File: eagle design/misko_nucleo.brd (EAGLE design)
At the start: 70 x 82.5 mm, 44 parts, among them IC1101 47309-2651, IC1201 FM25W256, IC1301 ADXL345, IC1302 74HCT1G32GW, IC401 TCAN334, J1 CAN, Q1701 SQ2310ES-T1_BE3, Q1702 SQ2310ES-T1_BE3, Q1703 SQ2310ES-T1_BE3

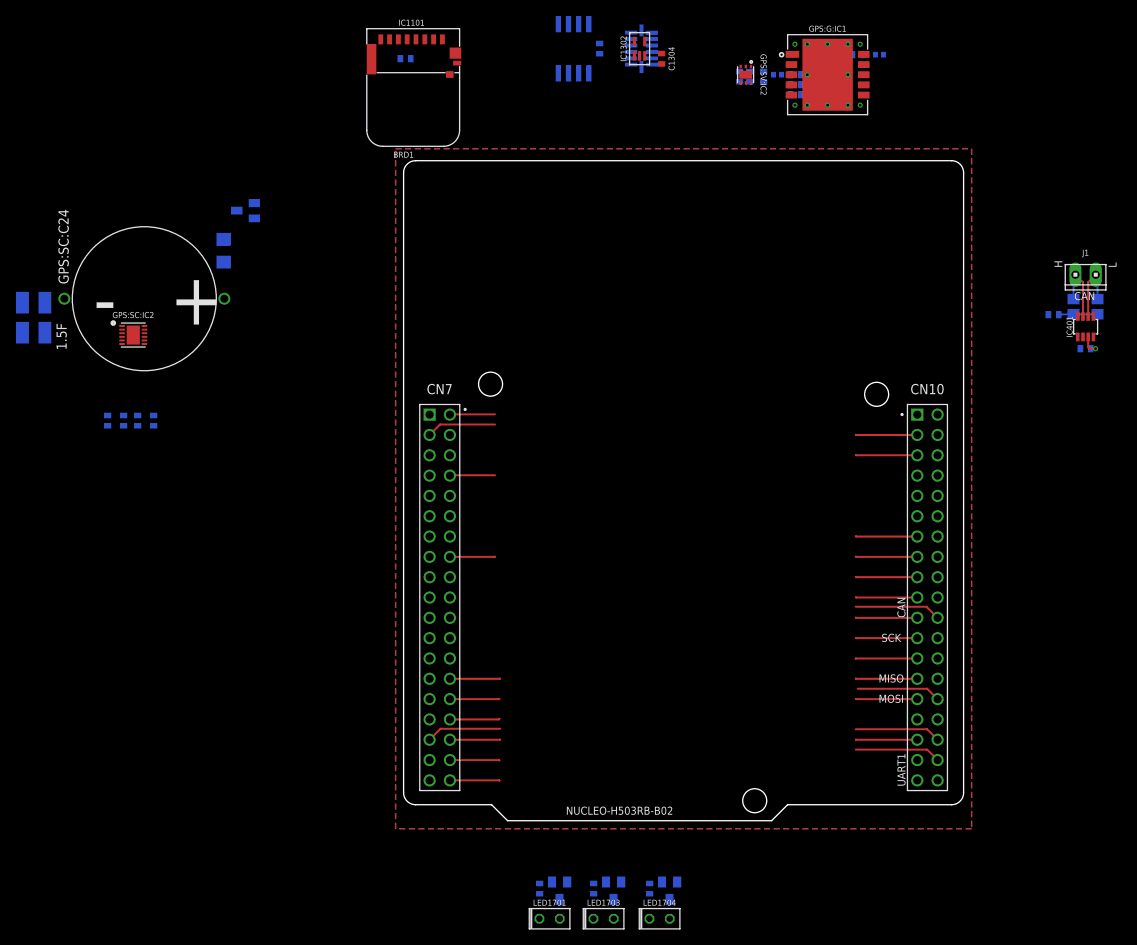
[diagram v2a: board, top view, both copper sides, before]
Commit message: board rev.3 on nucleo - connected & routed a nucleo H503RB-B02 compatible sch & brd - moved GPIOs to better suited physical locations - added yellow LED - sent board to the fab
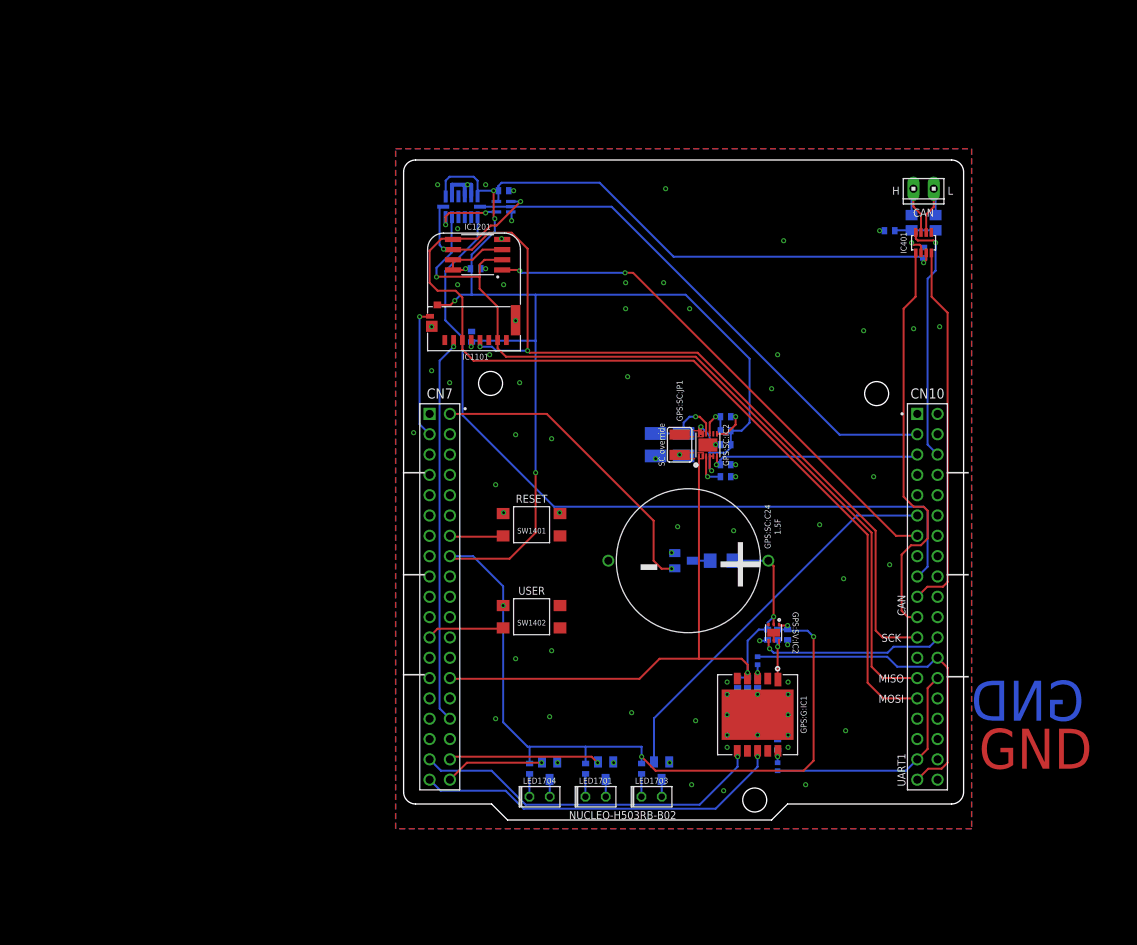
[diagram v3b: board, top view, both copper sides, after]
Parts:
- added GPS:SC:JP1: SC override, jumper:SJW
- added GPS:SC:R2: 10k, resistor:R0402
- added SW1401, SW1402: TL3305CF160QG, TL3305-844809 SPST-NO Tact Switch:SMD
- moved GPS:G:R2 89.9 mm to (46.8, 6.75), turned to 90 degrees
- moved GPS:G:C31 86.8 mm to (46.8, 9.50), turned to 90 degrees
- moved GPS:SC:C34 83.2 mm to (35.0, 47.0), turned to 90 degrees
- moved GPS:G:IC1 80.5 mm to (44.2, 13.2), turned to 270 degrees
- moved GPS:SC:C1 79.0 mm to (31.5, 47.0), turned to 270 degrees
- moved GPS:SC:R14 77.6 mm to (40.2, 43.0), turned to 0 degrees
- moved GPS:G:C22 76.1 mm to (44.2, 17.2), turned to 270 degrees
- moved GPS:SC:C24 75.5 mm to (35.8, 32.5)
- moved GPS:SC:C38 75.3 mm to (40.2, 47.0), turned to 0 degrees
- moved GPS:G:C2 75.0 mm to (43.0, 17.2), turned to 270 degrees
- moved GPS:G:C1 73.9 mm to (41.8, 17.2), turned to 270 degrees
- moved GPS:SC:R41 73.5 mm to (40.2, 50.5), turned to 0 degrees
- moved GPS:SC:R1 73.3 mm to (39.8, 32.5), turned to 180 degrees
- moved GPS:G:R1 73.3 mm to (44.2, 20.0), turned to 270 degrees
- moved GPS:SC:IC2 73.1 mm to (38.0, 47.0), turned to 90 degrees
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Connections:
- net GPS:SC:N$1 renamed GPS:SC:SC_DIS_DRAIN
- removed net GPS:SV:CT: GPS:SV:IC2.CT
- removed net GPS:VGPS: GPS:G:C1.1, GPS:G:C2.1, GPS:G:IC1.4_VCC, GPS:SC:C24.+, GPS:SC:C34.1, GPS:SC:IC2.VOUT1, GPS:SC:IC2.VOUT2, GPS:SC:R1.2, GPS:SV:C1.1, GPS:SV:IC2.SENSE
- removed net GPS_YELLOW_LED: BRD1.CN7_23
- removed net PA5: BRD1.CN10_11
- removed net PB1: BRD1.CN10_24
- removed net PC2: BRD1.CN7_35
- removed net PC3: BRD1.CN7_37
- removed net PC5: BRD1.CN10_6
- new net PA10: BRD1.CN10_33
- new net PA7: BRD1.CN10_15
- new net PB0: BRD1.CN7_34
- new net PB12: BRD1.CN10_16
- new net PC4: BRD1.CN10_34
- new net USER_BUTTON: BRD1.CN7_23, SW1402.1, SW1402.2
- net 3V3: now also GPS:SC:JP1.2, SW1402.3, SW1402.4
- net ADC_VGPS: now also GPS:G:C1.1, GPS:G:C2.1, GPS:G:IC1.4_VCC, GPS:SC:C24.+, GPS:SC:C34.1, GPS:SC:IC2.VOUT1, GPS:SC:IC2.VOUT2, GPS:SC:JP1.1, GPS:SC:R1.2, GPS:SV:C1.1, GPS:SV:IC2.SENSE
- net ADXL345_CS: now also BRD1.CN10_3; no longer BRD1.CN10_15
- net CAN_!STBY!: now also BRD1.CN10_6; no longer BRD1.CN10_16
- net GND: now also GPS:SC:R2.1, SW1401.3, SW1401.4
- net GPS_!RESET!: now also BRD1.CN7_37; no longer BRD1.CN10_3
- net GPS_PWR_CTRL: now also BRD1.CN10_24; no longer BRD1.CN10_34
- net GPS_WKUP: now also BRD1.CN7_35; no longer BRD1.CN10_33
- net LED_GREEN: now also BRD1.CN10_11; no longer BRD1.CN7_2
- net LED_RED: now also BRD1.CN7_38; no longer BRD1.CN7_3
- net LED_YELLOW: now also BRD1.CN7_36; no longer BRD1.CN7_38
- net NRST: now also SW1401.1, SW1401.2
- net SD_CD: now also BRD1.CN7_3; no longer BRD1.CN7_34
- net SPI1_MISO: no longer IC1101.CMD
- net SPI1_MOSI: now also IC1101.CMD
- net SUPERCAP_!EN!: now also GPS:SC:R2.2
- net SUPERCAP_DISCHARGE: now also BRD1.CN7_2; no longer BRD1.CN7_36
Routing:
- net 3V3: track 8.55 -> 313.4 mm, vias 1 -> 13
- net SPI1_MOSI: track 7.71 -> 116.4 mm, vias 0 -> 1
- net SPI1_SCK: track 7.71 -> 108.8 mm, vias 0 -> 3
- net SPI1_MISO: track 7.71 -> 107.5 mm, vias 0 -> 1
- net ADXL345_INT1: track 7.71 -> 99.2 mm
- net ADC_VGPS: track 6.29 -> 89.8 mm, vias 0 -> 3
- net ADXL345_CS: track 7.71 -> 66.5 mm
- net SPI1_FRAM_CS: track 7.71 -> 65.7 mm, vias 0 -> 2
- net CAN_TX: track 7.71 -> 51.7 mm
- net LED_GREEN: track 5.66 -> 48.9 mm
- net SPI1_SD_CS: track 6.25 -> 48.6 mm, vias 0 -> 1
- net GPS_MCU_TX: track 0.00 -> 41.8 mm
- net GPS_!RESET!: track 7.71 -> 46.7 mm, vias 0 -> 1
- net CAN_RX: track 7.71 -> 46.5 mm
- net GPS_WKUP: track 7.71 -> 44.8 mm, vias 0 -> 1
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- added copper zone on layer 1, net 3V3
- added copper zone on layer 1, net ADC_VGPS
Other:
- board text added: "GND"
- board text added: "RESET"
- board text added: "SC override"
- board text added: "USER"
- board text added: "docu"
- board text added: "|"
- board text removed: "info"

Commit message: - added BOM to rev3 board
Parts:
- C405: value 0.1uF / 10V -> 0.1u / 16V
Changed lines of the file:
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@@
 <attribute name="VALUE" x="67" y="72.25" size="0.5" layer="27" font="vector" rot="R90" align="center"/>
 </element>
-<element name="C405" library="rcl" library_urn="urn:adsk.eagle:library:334" package="C0402" package3d_urn="urn:adsk.eagle:package:23626/2" value="0.1uF / 10V" x="65" y="71" smashed="yes" rot="MR90">
+<element name="C405" library="rcl" library_urn="urn:adsk.eagle:library:334" package="C0402" package3d_urn="urn:adsk.eagle:package:23626/2" value="0.1u / 16V" x="65" y="71" smashed="yes" rot="MR90">
 <attribute name="NAME" x="63.75" y="71" size="0.75" layer="26" font="vector" rot="MR90" align="center"/>
 <attribute name="POPULARITY" value="18" x="65" y="71" size="0.75" layer="28" font="vector" rot="MR90" display="off"/>

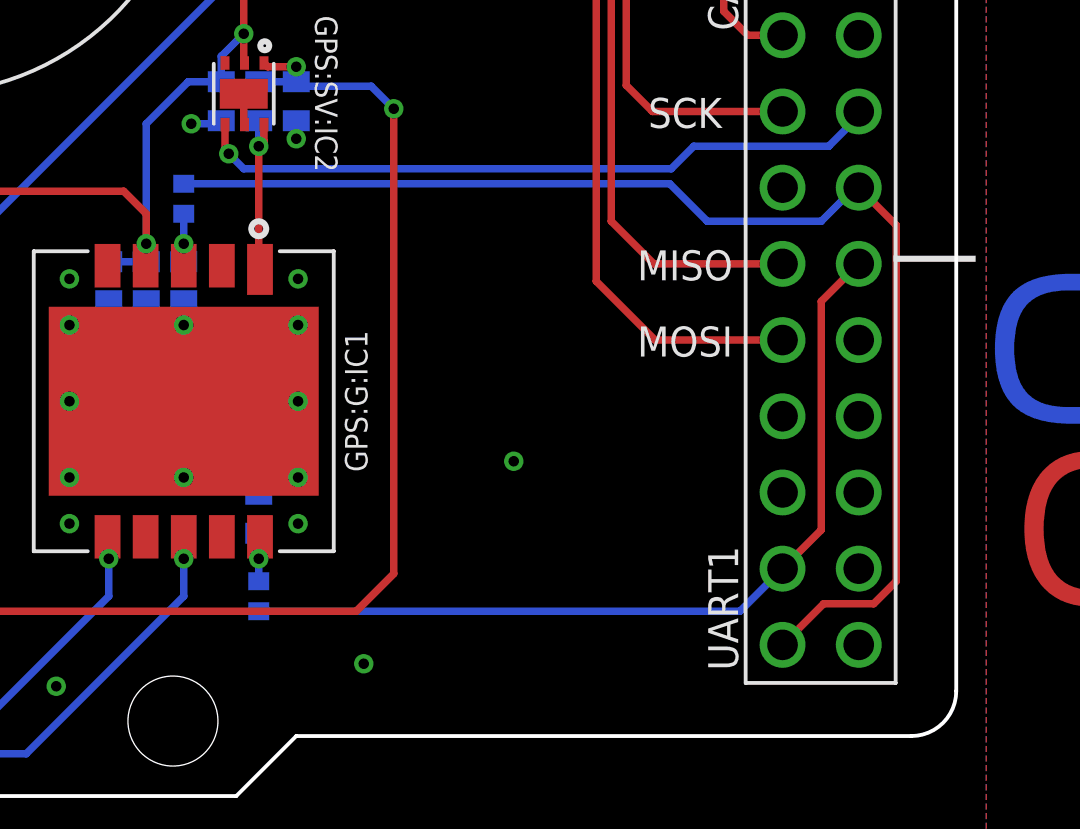
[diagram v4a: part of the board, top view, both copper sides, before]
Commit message: minor corrections for rev.3 board: - corrected UART1 lines towards board - added debug and attach launch configs - adapted code to match rev.3 board
- corrected BOM items
- renamed BOM
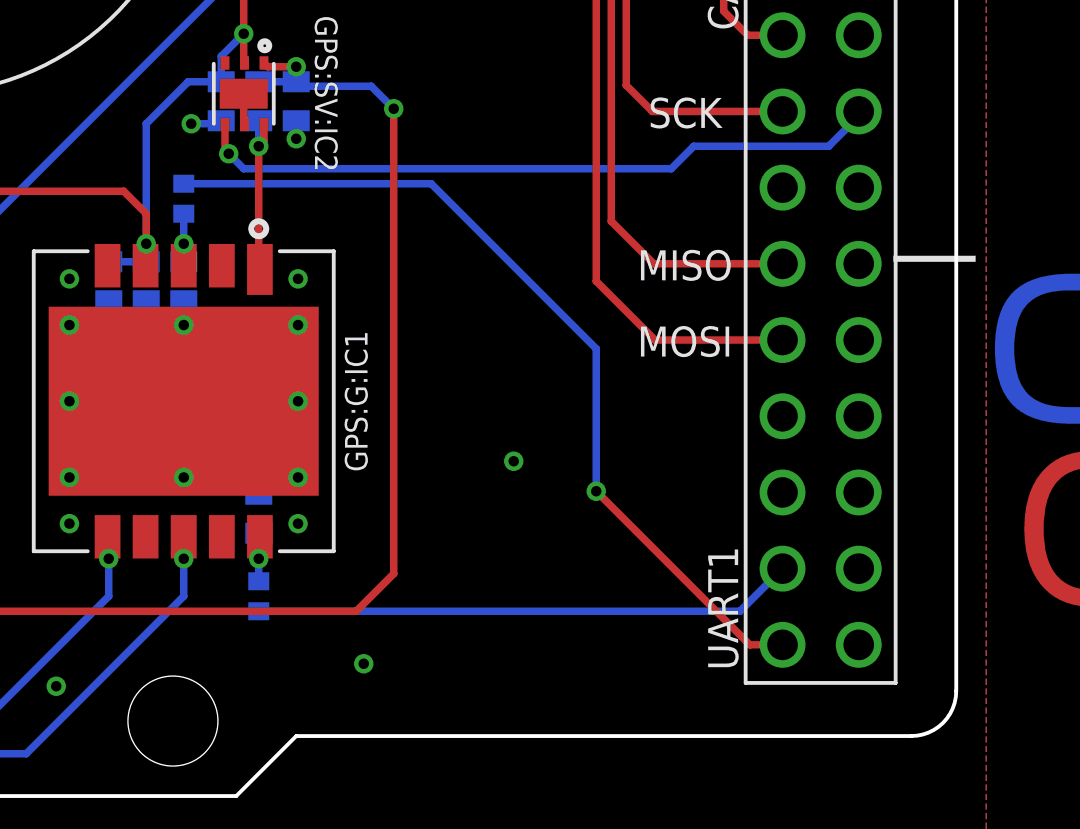
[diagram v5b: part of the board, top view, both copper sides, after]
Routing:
- net GPS_MCU_TX: track 41.8 -> 29.1 mm, vias 0 -> 1
- net GPS_MCU_RX: track 29.3 -> 18.0 mm
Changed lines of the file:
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@@
 <grid distance="0.25" unitdist="mm" unit="mm" style="lines" multiple="1" display="yes" altdistance="0.05" altunitdist="mm" altunit="mm"/>
 <layers>
-<layer number="1" name="Top" color="4" fill="1" visible="yes" active="yes"/>
+<layer number="1" name="Top" color="4" fill="1" visible="no" active="yes"/>
 <layer number="2" name="Route2" color="1" fill="3" visible="no" active="no"/>
 <layer number="3" name="Route3" color="4" fill="3" visible="no" active="no"/>
@@
 <layer number="14" name="Route14" color="1" fill="6" visible="no" active="no"/>
 <layer number="15" name="Route15" color="4" fill="6" visible="no" active="no"/>
-<layer number="16" name="Bottom" color="1" fill="1" visible="no" active="yes"/>
+<layer number="16" name="Bottom" color="1" fill="1" visible="yes" active="yes"/>
 <layer number="17" name="Pads" color="2" fill="1" visible="yes" active="yes"/>
 <layer number="18" name="Vias" color="2" fill="1" visible="yes" active="yes"/>
 <layer number="19" name="Unrouted" color="6" fill="1" visible="yes" active="yes"/>
 <layer number="20" name="Dimension" color="14" fill="1" visible="yes" active="yes"/>
-<layer number="21" name="tPlace" color="7" fill="1" visible="yes" active="yes"/>
-<layer number="22" name="bPlace" color="7" fill="1" visible="no" active="yes"/>
-<layer number="23" name="tOrigins" color="15" fill="1" visible="yes" active="yes"/>
-<layer number="24" name="bOrigins" color="15" fill="1" visible="no" active="yes"/>
-<layer number="25" name="tNames" color="7" fill="1" visible="yes" active="yes"/>
-<layer number="26" name="bNames" color="7" fill="1" visible="no" active="yes"/>
+<layer number="21" name="tPlace" color="7" fill="1" visible="no" active="yes"/>
+<layer number="22" name="bPlace" color="7" fill="1" visible="yes" active="yes"/>
+<layer number="23" name="tOrigins" color="15" fill="1" visible="no" active="yes"/>
+<layer number="24" name="bOrigins" color="15" fill="1" visible="yes" active="yes"/>
+<layer number="25" name="tNames" color="7" fill="1" visible="no" active="yes"/>
+<layer number="26" name="bNames" color="7" fill="1" visible="yes" active="yes"/>
 <layer number="27" name="tValues" color="7" fill="1" visible="no" active="yes"/>
 <layer number="28" name="bValues" color="7" fill="1" visible="no" active="yes"/>
-<layer number="29" name="tStop" color="7" fill="3" visible="yes" active="yes"/>
-<layer number="30" name="bStop" color="7" fill="6" visible="no" active="yes"/>
+<layer number="29" name="tStop" color="7" fill="3" visible="no" active="yes"/>
+<layer number="30" name="bStop" color="7" fill="6" visible="yes" active="yes"/>
 <layer number="31" name="tCream" color="7" fill="4" visible="no" active="yes"/>
 <layer number="32" name="bCream" color="7" fill="5" visible="no" active="yes"/>
@@
 <layer number="37" name="tTest" color="7" fill="1" visible="no" active="yes"/>
 <layer number="38" name="bTest" color="7" fill="1" visible="no" active="yes"/>
-<layer number="39" name="tKeepout" color="4" fill="11" visible="yes" active="yes"/>
-<layer number="40" name="bKeepout" color="1" fill="11" visible="no" active="yes"/>
-<layer number="41" name="tRestrict" color="4" fill="10" visible="yes" active="yes"/>
-<layer number="42" name="bRestrict" color="1" fill="10" visible="no" active="yes"/>
+<layer number="39" name="tKeepout" color="4" fill="11" visible="no" active="yes"/>
+<layer number="40" name="bKeepout" color="1" fill="11" visible="yes" active="yes"/>
+<layer number="41" name="tRestrict" color="4" fill="10" visible="no" active="yes"/>
+<layer number="42" name="bRestrict" color="1" fill="10" visible="yes" active="yes"/>
 <layer number="43" name="vRestrict" color="2" fill="10" visible="yes" active="yes"/>
 <layer number="44" name="Drills" color="7" fill="1" visible="no" active="yes"/>
@@
 <layer number="49" name="Reference" color="7" fill="1" visible="no" active="yes"/>
 <layer number="50" name="dxf" color="7" fill="1" visible="no" active="no"/>
-<layer number="51" name="tDocu" color="7" fill="1" visible="yes" active="yes"/>
-<layer number="52" name="bDocu" color="7" fill="1" visible="no" active="yes"/>
+<layer number="51" name="tDocu" color="7" fill="1" visible="no" active="yes"/>
+<layer number="52" name="bDocu" color="7" fill="1" visible="yes" active="yes"/>
 <layer number="53" name="tGND_GNDA" color="7" fill="9" visible="no" active="no"/>
 <layer number="54" name="bGND_GNDA" color="1" fill="9" visible="no" active="no"/>
@@
 <wire x1="64.21" y1="7.67" x2="62.79" y2="6.25" width="0.25" layer="16"/>
 <wire x1="62.79" y1="6.25" x2="46.75" y2="6.25" width="0.25" layer="16"/>
-<wire x1="64.21" y1="7.67" x2="65.5" y2="8.96" width="0.25" layer="1"/>
-<wire x1="65.5" y1="16.58" x2="66.75" y2="17.83" width="0.25" layer="1"/>
-<wire x1="65.5" y1="8.96" x2="65.5" y2="16.58" width="0.25" layer="1"/>
+<wire x1="64.21" y1="7.67" x2="66.75" y2="17.83" width="0" layer="19" extent="1-1"/>
 </signal>
 <signal name="GPS_MCU_TX" class="2">
@@
 <contactref element="BRD1" pad="CN10_26"/>
 <contactref element="GPS:G:R1" pad="1"/>
-<wire x1="44.25" y1="20.5" x2="60.44850625" y2="20.5" width="0.25" layer="16"/>
-<wire x1="60.44850625" y1="20.5" x2="61.69850625" y2="19.25" width="0.25" layer="16"/>
-<wire x1="66.75" y1="20.37" x2="66.62" y2="20.37" width="0.25" layer="16"/>
-<wire x1="66.62" y1="20.37" x2="65.5" y2="19.25" width="0.25" layer="16"/>
-<wire x1="65.5" y1="19.25" x2="61.69850625" y2="19.25" width="0.25" layer="16"/>
-<wire x1="64.21" y1="5.13" x2="65.58" y2="6.5" width="0.25" layer="1"/>
-<wire x1="67.25" y1="6.5" x2="68" y2="7.25" width="0.25" layer="1"/>
-<wire x1="68" y1="19.12" x2="66.75" y2="20.37" width="0.25" layer="1"/>
-<wire x1="65.58" y1="6.5" x2="67.25" y2="6.5" width="0.25" layer="1"/>
-<wire x1="68" y1="7.25" x2="68" y2="19.12" width="0.25" layer="1"/>
+<wire x1="44.25" y1="20.5" x2="52.5" y2="20.5" width="0.25" layer="16"/>
+<wire x1="52.5" y1="20.5" x2="58" y2="15" width="0.25" layer="16"/>
+<via x="58" y="10.25" extent="1-16" drill="0.35"/>
+<wire x1="58" y1="10.25" x2="63.12" y2="5.13" width="0.25" layer="1"/>
+<wire x1="63.12" y1="5.13" x2="64.21" y2="5.13" width="0.25" layer="1"/>
+<wire x1="58" y1="15" x2="58" y2="10.25" width="0.25" layer="16"/>
+<wire x1="58" y1="10.25" x2="66.75" y2="20.37" width="0" layer="19" extent="1-1"/>
 </signal>
 <signal name="VBAT" class="2">
